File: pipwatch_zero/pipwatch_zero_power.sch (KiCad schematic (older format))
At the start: 18 parts, among them U201 MICRO-B_USB, U202 USB6BX, U203 MCP73831, U204 LD59015C33R

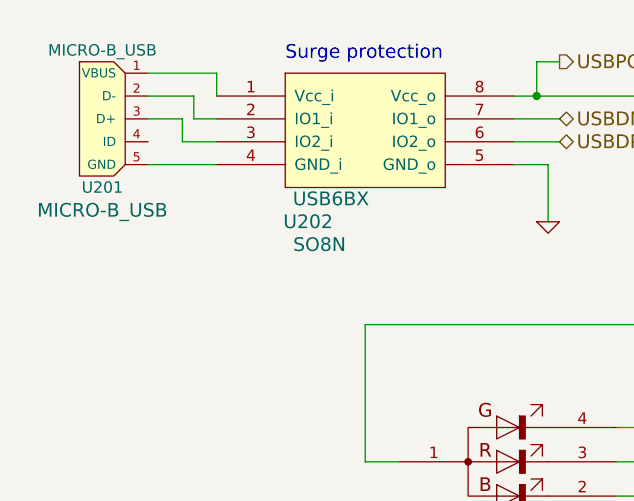
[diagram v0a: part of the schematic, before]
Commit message: hw drawing (started), sw fixes for presentation
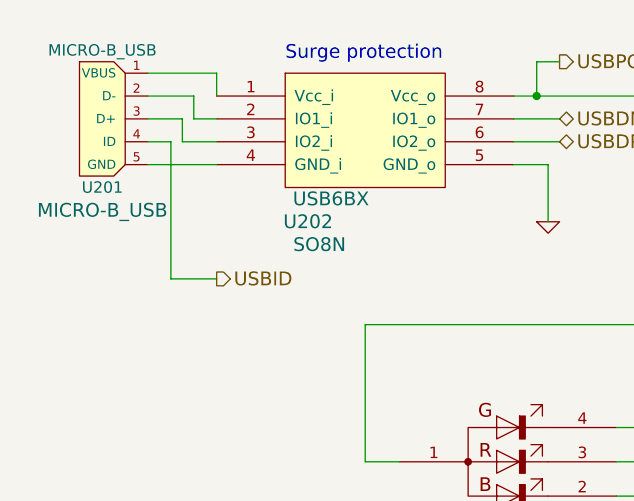
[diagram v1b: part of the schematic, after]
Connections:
- net USBID: now reaches U201.4 (ID)
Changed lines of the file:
@@
 Sheet 2 3
 Title ""
-Date "29 jul 2014"
+Date "30 jul 2014"
 Rev ""
 Comp ""
@@
 Text Notes 8750 2950 0    60   ~ 0
 Low-Drop Regulator
+Text HLabel 1800 3900 2    60   Output ~ 0
+USBID
+Wire Wire Line
+	1500 3300 1600 3300
+Wire Wire Line
+	1600 3300 1600 3900
+Wire Wire Line
+	1600 3900 1800 3900
 $EndSCHEMATC

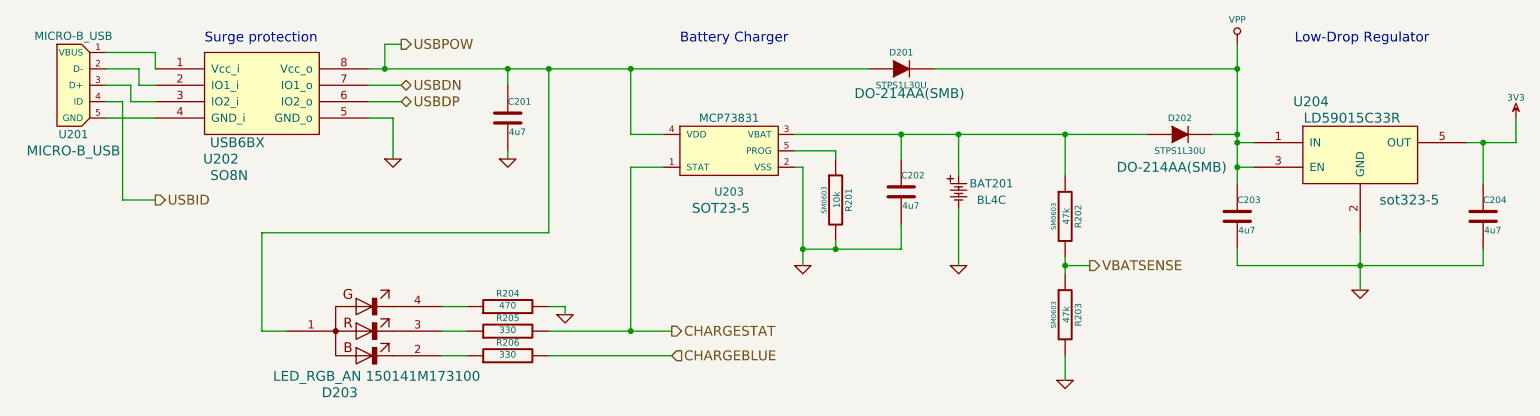
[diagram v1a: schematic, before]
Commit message: pipwatch_zero: basic schema complete
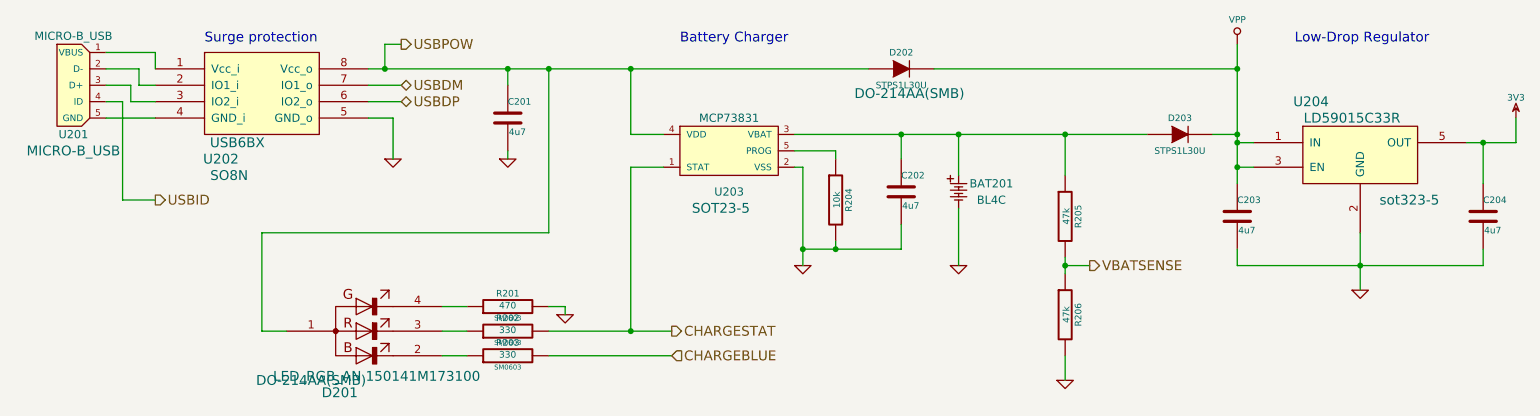
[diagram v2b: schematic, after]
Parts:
- D201: renamed from D203; footprint (none) -> DO-214AA(SMB)
- D203: renamed from D202; footprint DO-214AA(SMB) -> (none)
- R201: renamed from R204; footprint (none) -> SM0603
- R202: renamed from R205; footprint (none) -> SM0603
- R203: renamed from R206; footprint (none) -> SM0603
- R204: renamed from R201; footprint SM0603 -> (none)
- R205: renamed from R202; footprint SM0603 -> (none)
- R206: renamed from R203; footprint SM0603 -> (none)
- renumbered D201 to D202
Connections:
- net USBDN renamed USBDM
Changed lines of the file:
@@
 LIBS:open-project
 LIBS:misc_pip
+LIBS:misc_epd
 LIBS:pipwatch_zero-cache
 EELAYER 27 0
@@
 $Descr A4 11693 8268
 encoding utf-8
-Sheet 2 3
+Sheet 2 5
 Title ""
-Date "30 jul 2014"
+Date "23 aug 2014"
 Rev ""
 Comp ""
@@
 	3100 3300 3300 3300
 Text HLabel 3300 3200 2    60   BiDi ~ 0
-USBDN
+USBDM
 Text HLabel 3300 3300 2    60   BiDi ~ 0
 USBDP
@@
 	3100 3100 6150 3100
 $Comp
-L GND #PWR201
+L GND #PWR01
 U 1 1 53D80678
 P 3250 3650
-F 0 "#PWR201" H 3250 3650 30  0001 C CNN
+F 0 "#PWR01" H 3250 3650 30  0001 C CNN
 F 1 "GND" H 3250 3580 30  0001 C CNN
 F 2 "" H 3250 3650 60  0000 C CNN
@@
 	3950 3100 3950 3200
 $Comp
-L GND #PWR202
+L GND #PWR02
 U 1 1 53D80768
 P 3950 3650
-F 0 "#PWR202" H 3950 3650 30  0001 C CNN
+F 0 "#PWR02" H 3950 3650 30  0001 C CNN
 F 1 "GND" H 3950 3580 30  0001 C CNN
 F 2 "" H 3950 3650 60  0000 C CNN
@@
 $EndComp
 $Comp
-L GND #PWR204
+L GND #PWR03
 U 1 1 53D809FA
 P 5750 4300
-F 0 "#PWR204" H 5750 4300 30  0001 C CNN
+F 0 "#PWR03" H 5750 4300 30  0001 C CNN
 F 1 "GND" H 5750 4230 30  0001 C CNN
 F 2 "" H 5750 4300 60  0000 C CNN
@@
 	5750 3700 5750 4300
 $Comp
-L R R201
+L R R204
 U 1 1 53D80AFA
 P 5950 3900
-F 0 "R201" V 6030 3900 40  0000 C CNN
+F 0 "R204" V 6030 3900 40  0000 C CNN
 F 1 "10k" V 5957 3901 40  0000 C CNN
-F 2 "SM0603" V 5880 3900 30  0000 C CNN
+F 2 "" V 5880 3900 30  0000 C CNN
 F 3 "~" H 5950 3900 30  0000 C CNN
 	1    5950 3900
@@
 	8400 3700 8500 3700
 $Comp
-L GND #PWR208
+L GND #PWR04
 U 1 1 53D80B65
 P 9150 4450
-F 0 "#PWR208" H 9150 4450 30  0001 C CNN
+F 0 "#PWR04" H 9150 4450 30  0001 C CNN
 F 1 "GND" H 9150 4380 30  0001 C CNN
 F 2 "" H 9150 4450 60  0000 C CNN
@@
 $EndComp
 $Comp
-L DIODE D201
+L DIODE D202
 U 1 1 53D80C1A
 P 6350 3100
-F 0 "D201" H 6350 3200 40  0000 C CNN
+F 0 "D202" H 6350 3200 40  0000 C CNN
 F 1 "STPS1L30U" H 6350 3000 40  0000 C CNN
 F 2 "DO-214AA(SMB)" H 6400 2950 60  0000 C CNN
@@
 	6700 3500 6700 3750
 $Comp
-L DIODE D202
+L DIODE D203
 U 1 1 53D80D12
 P 8050 3500
-F 0 "D202" H 8050 3600 40  0000 C CNN
+F 0 "D203" H 8050 3600 40  0000 C CNN
 F 1 "STPS1L30U" H 8050 3400 40  0000 C CNN
-F 2 "DO-214AA(SMB)" H 8000 3300 60  0000 C CNN
+F 2 "" H 8000 3300 60  0000 C CNN
 F 3 "~" H 8050 3500 60  0000 C CNN
 	1    8050 3500
@@
 Connection ~ 5950 4200
 $Comp
-L GND #PWR205
+L GND #PWR05
 U 1 1 53D80E9B
 P 6700 4300
-F 0 "#PWR205" H 6700 4300 30  0001 C CNN
+F 0 "#PWR05" H 6700 4300 30  0001 C CNN
 F 1 "GND" H 6700 4230 30  0001 C CNN
 F 2 "" H 6700 4300 60  0000 C CNN
@@
 	6700 3950 6700 4300
 $Comp
-L R R202
+L R R205
 U 1 1 53D80F08
 P 7350 4000
-F 0 "R202" V 7430 4000 40  0000 C CNN
+F 0 "R205" V 7430 4000 40  0000 C CNN
 F 1 "47k" V 7357 4001 40  0000 C CNN
-F 2 "SM0603" V 7280 4000 30  0000 C CNN
+F 2 "" V 7280 4000 30  0000 C CNN
 F 3 "~" H 7350 4000 30  0000 C CNN
 	1    7350 4000
@@
 $EndComp
 $Comp
-L R R203
+L R R206
 U 1 1 53D80F21
 P 7350 4600
-F 0 "R203" V 7430 4600 40  0000 C CNN
+F 0 "R206" V 7430 4600 40  0000 C CNN
 F 1 "47k" V 7357 4601 40  0000 C CNN
-F 2 "SM0603" V 7280 4600 30  0000 C CNN
+F 2 "" V 7280 4600 30  0000 C CNN
 F 3 "~" H 7350 4600 30  0000 C CNN
 	1    7350 4600
@@
 	7350 4250 7350 4350
 $Comp
-L GND #PWR206
+L GND #PWR06
 U 1 1 53D80F8F
 P 7350 5000
-F 0 "#PWR206" H 7350 5000 30  0001 C CNN
+F 0 "#PWR06" H 7350 5000 30  0001 C CNN
 F 1 "GND" H 7350 4930 30  0001 C CNN
 F 2 "" H 7350 5000 60  0000 C CNN
@@
 $EndComp
 $Comp
-L 3V3 #PWR209
+L 3V3 #PWR07
 U 1 1 53D81207
 P 10100 3400
-F 0 "#PWR209" H 10100 3500 40  0001 C CNN
+F 0 "#PWR07" H 10100 3500 40  0001 C CNN
 F 1 "3V3" H 10100 3525 40  0000 C CNN
 F 2 "" H 10100 3400 60  0000 C CNN
@@
 	4700 3700 4900 3700
 $Comp
-L LED_RGB_AN D203
+L LED_RGB_AN D201
 U 1 1 53D82AB0
 P 2900 4700
-F 0 "D203" H 2925 4325 60  0000 C CNN
+F 0 "D201" H 2925 4325 60  0000 C CNN
 F 1 "LED_RGB_AN 150141M173100" H 3150 4425 60  0000 C CNN
-F 2 "" H 2750 4400 60  0000 C CNN
+F 2 "DO-214AA(SMB)" H 2750 4400 60  0000 C CNN
 F 3 "" H 2750 4400 60  0000 C CNN
 	1    2900 4700
@@
 $EndComp
 $Comp
-L R R204
+L R R201
 U 1 1 53D82ABF
 P 3950 4550
-F 0 "R204" V 4030 4550 40  0000 C CNN
+F 0 "R201" V 4030 4550 40  0000 C CNN
 F 1 "470" V 3957 4551 40  0000 C CNN
-F 2 "" V 3880 4550 30  0000 C CNN
+F 2 "SM0603" V 3880 4550 30  0000 C CNN
 F 3 "~" H 3950 4550 30  0000 C CNN
 	1    3950 4550
@@
 $EndComp
 $Comp
-L R R205
+L R R202
 U 1 1 53D82ACE
 P 3950 4700
-F 0 "R205" V 4030 4700 40  0000 C CNN
+F 0 "R202" V 4030 4700 40  0000 C CNN
 F 1 "330" V 3957 4701 40  0000 C CNN
-F 2 "" V 3880 4700 30  0000 C CNN
+F 2 "SM0603" V 3880 4700 30  0000 C CNN
 F 3 "~" H 3950 4700 30  0000 C CNN
 	1    3950 4700
@@
 Connection ~ 4700 4700
 $Comp
-L R R206
+L R R203
 U 1 1 53D82BFA
 P 3950 4850
-F 0 "R206" V 4030 4850 40  0000 C CNN
+F 0 "R203" V 4030 4850 40  0000 C CNN
 F 1 "330" V 3957 4851 40  0000 C CNN
-F 2 "" V 3880 4850 30  0000 C CNN
+F 2 "SM0603" V 3880 4850 30  0000 C CNN
 F 3 "~" H 3950 4850 30  0000 C CNN
 	1    3950 4850
@@
 $EndComp
 $Comp
-L GND #PWR203
+L GND #PWR08
 U 1 1 53D82C48
 P 4300 4600
-F 0 "#PWR203" H 4300 4600 30  0001 C CNN
+F 0 "#PWR08" H 4300 4600 30  0001 C CNN
 F 1 "GND" H 4300 4530 30  0001 C CNN
 F 2 "" H 4300 4600 60  0000 C CNN

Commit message: pipwatch_zero: footprints
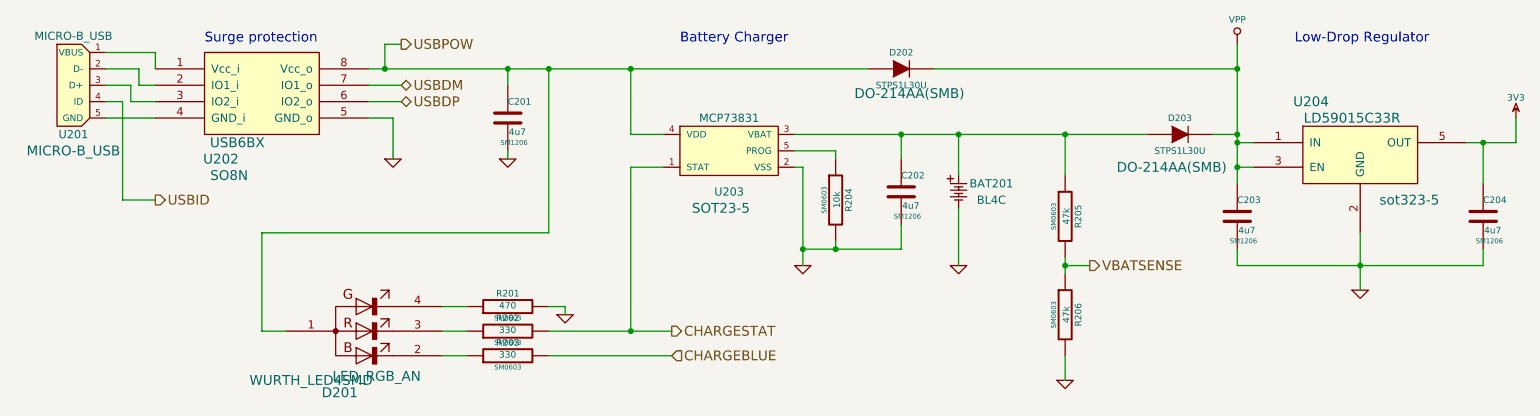
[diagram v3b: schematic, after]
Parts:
- BAT201: footprint PIN_ARRAY_2X1 -> do214aa
- C201, C202, C203, C204: footprint (none) -> SM1206
- D201: value LED_RGB_AN 150141M173100 -> LED_RGB_AN; footprint DO-214AA(SMB) -> WURTH_LED4SMD
- D203: footprint (none) -> DO-214AA(SMB)
- R204, R205, R206: footprint (none) -> SM0603
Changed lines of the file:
@@
 Sheet 2 5
 Title ""
-Date "23 aug 2014"
+Date "24 aug 2014"
 Rev ""
 Comp ""
@@
 F 0 "C201" H 3950 3500 40  0000 L CNN
 F 1 "4u7" H 3956 3315 40  0000 L CNN
-F 2 "" H 3988 3250 30  0000 C CNN
+F 2 "SM1206" H 3988 3250 30  0000 C CNN
 F 3 "~" H 3950 3400 60  0000 C CNN
 	1    3950 3400
@@
 F 0 "R204" V 6030 3900 40  0000 C CNN
 F 1 "10k" V 5957 3901 40  0000 C CNN
-F 2 "" V 5880 3900 30  0000 C CNN
+F 2 "SM0603" V 5880 3900 30  0000 C CNN
 F 3 "~" H 5950 3900 30  0000 C CNN
 	1    5950 3900
@@
 F 0 "BAT201" H 6900 3900 50  0000 C CNN
 F 1 "BL4C" H 6900 3800 50  0000 C CNN
-F 2 "PIN_ARRAY_2X1" V 6850 3400 60  0001 C CNN
+F 2 "do214aa" V 6850 3400 60  0001 C CNN
 F 3 "" H 6700 3850 60  0000 C CNN
 	1    6700 3850
@@
 F 0 "C202" H 6350 3950 40  0000 L CNN
 F 1 "4u7" H 6356 3765 40  0000 L CNN
-F 2 "" H 6388 3700 30  0000 C CNN
+F 2 "SM1206" H 6388 3700 30  0000 C CNN
 F 3 "~" H 6350 3850 60  0000 C CNN
 	1    6350 3850
@@
 F 0 "D203" H 8050 3600 40  0000 C CNN
 F 1 "STPS1L30U" H 8050 3400 40  0000 C CNN
-F 2 "" H 8000 3300 60  0000 C CNN
+F 2 "DO-214AA(SMB)" H 8000 3300 60  0000 C CNN
 F 3 "~" H 8050 3500 60  0000 C CNN
 	1    8050 3500
@@
 F 0 "C203" H 8400 4100 40  0000 L CNN
 F 1 "4u7" H 8406 3915 40  0000 L CNN
-F 2 "" H 8438 3850 30  0000 C CNN
+F 2 "SM1206" H 8438 3850 30  0000 C CNN
 F 3 "~" H 8400 4000 60  0000 C CNN
 	1    8400 4000
@@
 F 0 "C204" H 9900 4100 40  0000 L CNN
 F 1 "4u7" H 9906 3915 40  0000 L CNN
-F 2 "" H 9938 3850 30  0000 C CNN
+F 2 "SM1206" H 9938 3850 30  0000 C CNN
 F 3 "~" H 9900 4000 60  0000 C CNN
 	1    9900 4000
@@
 F 0 "R205" V 7430 4000 40  0000 C CNN
 F 1 "47k" V 7357 4001 40  0000 C CNN
-F 2 "" V 7280 4000 30  0000 C CNN
+F 2 "SM0603" V 7280 4000 30  0000 C CNN
 F 3 "~" H 7350 4000 30  0000 C CNN
 	1    7350 4000
@@
 F 0 "R206" V 7430 4600 40  0000 C CNN
 F 1 "47k" V 7357 4601 40  0000 C CNN
-F 2 "" V 7280 4600 30  0000 C CNN
+F 2 "SM0603" V 7280 4600 30  0000 C CNN
 F 3 "~" H 7350 4600 30  0000 C CNN
 	1    7350 4600
@@
 P 2900 4700
 F 0 "D201" H 2925 4325 60  0000 C CNN
-F 1 "LED_RGB_AN 150141M173100" H 3150 4425 60  0000 C CNN
-F 2 "DO-214AA(SMB)" H 2750 4400 60  0000 C CNN
+F 1 "LED_RGB_AN" H 3150 4425 60  0000 C CNN
+F 2 "WURTH_LED4SMD" H 2750 4400 60  0000 C CNN
 F 3 "" H 2750 4400 60  0000 C CNN
 	1    2900 4700
